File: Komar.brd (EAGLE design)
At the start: 58 x 58 mm, 109 parts, among them CON1 USB-VERTICAL, CON2 PINHEAD_1X01-2, CON3 CON-4P-TABS-STRAIGHT, CON4 CON-4P-TABS-STRAIGHT, CON5 CON-4P-TABS-STRAIGHT, CON6 CON-4P-TABS-STRAIGHT, CON7 CON-4P-TABS-STRAIGHT, CON8 CON-6P-SM06B, CON9 PINHEAD_1X01-2, IC1 TPD3S014DBVR-SOT23-6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

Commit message: CAN transciever replaced due for logistic reasons
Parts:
- IC3, IC4: value TJA1051-HVSON8 -> ATA6561-GBQW-N-HVSON8

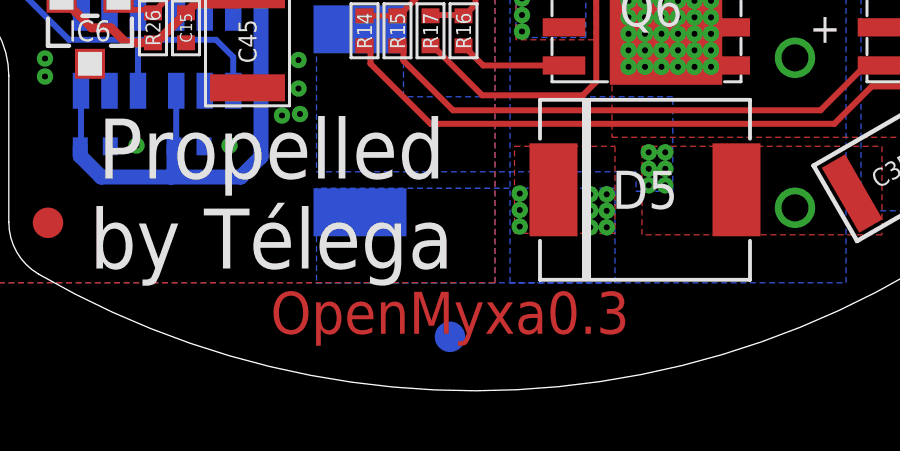
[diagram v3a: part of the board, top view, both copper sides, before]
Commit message: NETs naming updates
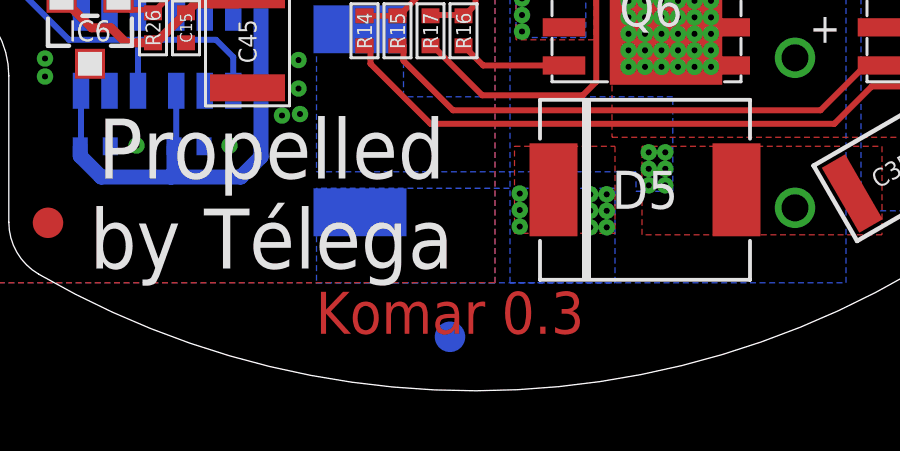
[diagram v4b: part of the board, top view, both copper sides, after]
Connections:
- net N$1 renamed BGH2
- net N$11 renamed AGL1
- net N$12 renamed CGH2
- net N$13 renamed CGL2
- net N$14 renamed CGH1
- net N$15 renamed CGL1
- net N$2 renamed BGL2
- net N$3 renamed BGL1
- net N$4 renamed BGH1
- net N$7 renamed AGH2
- net N$8 renamed AGL2
- net N$9 renamed AGH1
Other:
- board text added: "Komar 0.3"
- board text removed: "OpenMyxa0.3"
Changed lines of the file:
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@@
 <plain>
 <wire x1="29.2" y1="56.85" x2="29.2" y2="1.15" width="0.2" layer="22" style="shortdash"/>
-<text x="28.2" y="2.6" size="1.4" layer="1" font="vector" ratio="15" align="center">OpenMyxa0.3</text>
+<text x="28.2" y="2.6" size="1.4" layer="1" font="vector" ratio="15" align="center">Komar 0.3</text>
 <wire x1="16.5" y1="3.6" x2="40" y2="3.6" width="0.1" layer="49"/>
 <text x="22.25" y="6.575" size="2" layer="21" font="vector" ratio="15" align="center">Propelled
@@
 <wire x1="26.4" y1="45.025" x2="26.475" y2="45.1" width="0.4" layer="1"/>
 </signal>
-<signal name="N$1" class="1">
+<signal name="BGH2" class="1">
 <contactref element="Q1" pad="4"/>
 <contactref element="R2" pad="2"/>
@@
 <wire x1="28" y1="14" x2="28" y2="16" width="0.2" layer="1"/>
 </signal>
-<signal name="N$2">
+<signal name="BGL2">
 <contactref element="Q2" pad="4"/>
 <contactref element="R3" pad="2"/>
@@
 <wire x1="29.05" y1="18.95" x2="28" y2="20" width="0.2" layer="1"/>
 </signal>
-<signal name="N$4" class="1">
+<signal name="BGH1" class="1">
 <contactref element="Q3" pad="4"/>
 <contactref element="R1" pad="2"/>
@@
 <wire x1="26.55" y1="25" x2="27.225" y2="25" width="0.2" layer="16"/>
 </signal>
-<signal name="N$3">
+<signal name="BGL1">
 <contactref element="R4" pad="2"/>
 <contactref element="Q4" pad="4"/>
@@
 <wire x1="24.75" y1="29.8364" x2="24.75" y2="27.1" width="0.2" layer="15"/>
 </signal>
-<signal name="N$7" class="1">
+<signal name="AGH2" class="1">
 <contactref element="Q5" pad="4"/>
 <contactref element="R15" pad="2"/>
@@
 <wire x1="42.045" y1="10.845" x2="40.55" y2="9.35" width="0.2" layer="1"/>
 </signal>
-<signal name="N$8">
+<signal name="AGL2">
 <contactref element="Q6" pad="4"/>
 <contactref element="R16" pad="2"/>
@@
 <wire x1="28.65" y1="11.5" x2="29.305" y2="10.845" width="0.2" layer="1"/>
 </signal>
-<signal name="N$9" class="1">
+<signal name="AGH1" class="1">
 <contactref element="Q7" pad="4"/>
 <contactref element="R14" pad="2"/>
@@
 <wire x1="43.65" y1="16.85" x2="43.3" y2="17.2" width="0.2" layer="1"/>
 </signal>
-<signal name="N$11">
+<signal name="AGL1">
 <contactref element="R17" pad="2"/>
 <contactref element="Q8" pad="4"/>
@@
 <wire x1="23.5" y1="43" x2="23.70606875" y2="43" width="0.15" layer="16"/>
 </signal>
-<signal name="N$12" class="1">
+<signal name="CGH2" class="1">
 <contactref element="Q9" pad="4"/>
 <contactref element="R22" pad="2"/>
@@
 <wire x1="26.375" y1="30.45" x2="26.375" y2="29.8" width="0.15" layer="16"/>
 </signal>
-<signal name="N$13">
+<signal name="CGL2">
 <contactref element="Q10" pad="4"/>
 <contactref element="R23" pad="2"/>
@@
 <wire x1="26.2" y1="26.725425" x2="26.2" y2="28.825" width="0.2" layer="15"/>
 </signal>
-<signal name="N$14" class="1">
+<signal name="CGH1" class="1">
 <contactref element="Q11" pad="4"/>
 <contactref element="R21" pad="2"/>
@@
 <wire x1="42.575" y1="30.525" x2="42.45" y2="30.4" width="0.2" layer="1"/>
 </signal>
-<signal name="N$15">
+<signal name="CGL1">
 <contactref element="R24" pad="2"/>
 <contactref element="Q12" pad="4"/>

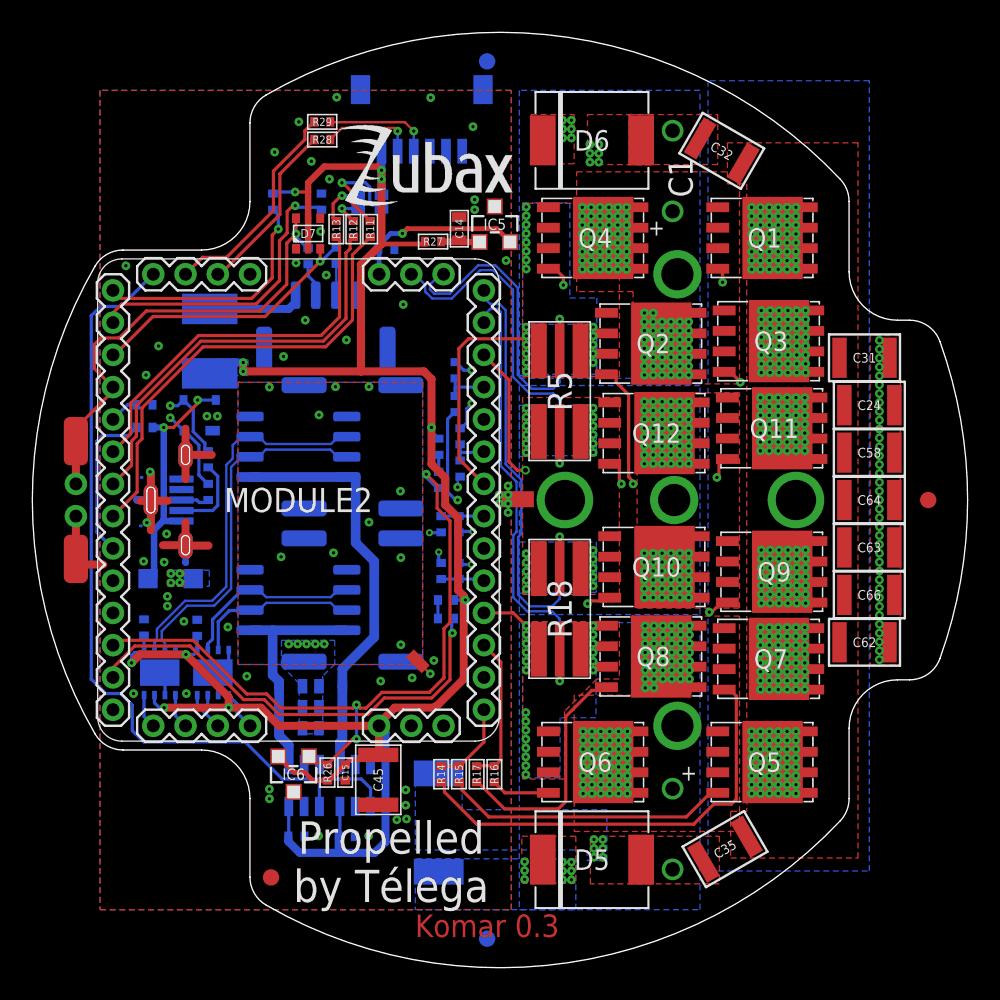
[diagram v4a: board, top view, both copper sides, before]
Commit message: powerstage rerouting partially completed
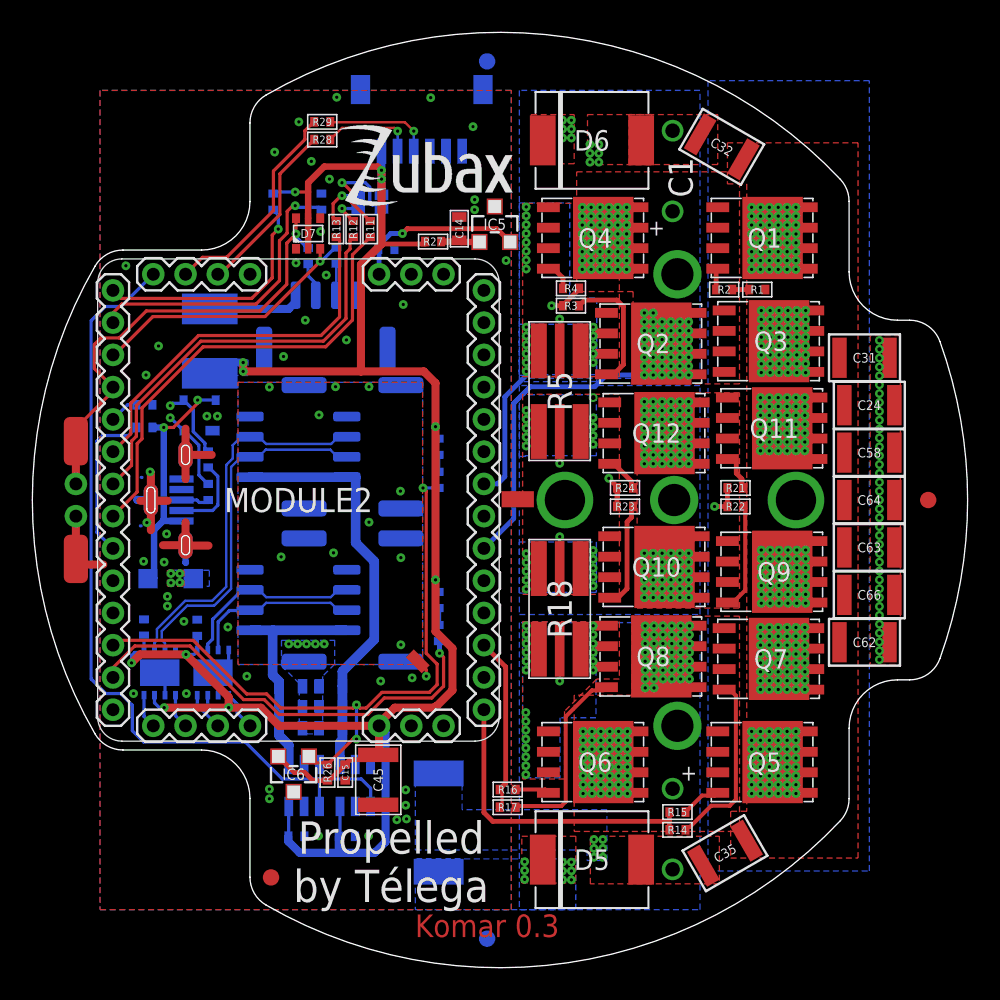
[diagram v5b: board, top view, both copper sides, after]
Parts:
- moved R1 25.4 mm to (45.0, 42.0), flipped to the top, turned to 0 degrees
- moved R2 24.7 mm to (42.9, 42.0), flipped to the top, turned to 180 degrees
- moved R21 17.4 mm to (43.6, 29.8), flipped to the top, turned to 0 degrees
- moved R22 17.2 mm to (43.6, 28.6), flipped to the top, turned to 0 degrees
- moved R4 16.7 mm to (33.4, 42.1), flipped to the top, turned to 180 degrees
- moved R3 15.2 mm to (33.4, 41.0), flipped to the top, turned to 0 degrees
- moved R14 15.1 mm to (40.0, 8.55), turned to 0 degrees
- moved R15 13.8 mm to (40.0, 9.65), turned to 0 degrees
- moved R24 12.8 mm to (36.8, 29.8), flipped to the top, turned to 0 degrees
- moved R23 12.3 mm to (36.8, 28.6), flipped to the top, turned to 0 degrees
- moved S1 6.16 mm to (34.8, 35.4)
- moved R17 2.81 mm to (29.5, 9.95), turned to 0 degrees
- moved R16 1.26 mm to (29.5, 11.1), turned to 0 degrees
- moved R9 1.01 mm to (25.2, 20.8), turned to 90 degrees
- moved LED1 0.45 mm to (25.2, 22.8), turned to 270 degrees
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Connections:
- net BGH2 renamed JHKJ
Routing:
- net JHKJ: track 34.3 -> 1.64 mm, vias 2 -> 0
- net PHASE_B_GATE_HIGH: track 2.69 -> 35.3 mm
- net BGH1: track 28.1 -> 0.00 mm, vias 2 -> 0
- net BGL1: track 25.4 -> 1.79 mm, vias 2 -> 0
- net CGH1: track 23.6 -> 2.39 mm, vias 2 -> 0
- net CGH2: track 26.9 -> 6.65 mm, vias 2 -> 0
- net PHASE_B_GATE_LOW: track 2.65 -> 20.0 mm, vias 0 -> 1
- net CGL1: track 20.0 -> 2.85 mm, vias 2 -> 0
- net PHASE_C_GATE_HIGH: track 2.52 -> 19.0 mm, vias 0 -> 1
- net AGH1: track 27.6 -> 11.2 mm
- net AGH2: track 17.9 -> 2.69 mm
- net CGL2: track 21.3 -> 6.84 mm, vias 2 -> 0
- net PHASE_A_GATE_HIGH: track 5.36 -> 19.2 mm
- net BGL2: track 20.6 -> 7.96 mm, vias 2 -> 0
- net PHASE_C_GATE_LOW: track 3.41 -> 12.0 mm, vias 0 -> 1
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
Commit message: Routing completed
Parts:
- moved R1 0.15 mm to (45.1, 42.0), turned to 180 degrees
- turned R2 to 0 degrees
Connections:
- net JHKJ renamed BGH2
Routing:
- net BGH1: track 0.00 -> 6.24 mm
- net PHASE_B_GATE_HIGH: track 35.3 -> 40.2 mm, vias 0 -> 2
- net CGL1: track 2.85 -> 2.25 mm

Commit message: minor tweaks
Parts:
- moved R3 0.47 mm to (33.8, 40.8)
- moved R4 0.46 mm to (33.8, 41.9)
- moved R21 0.05 mm to (43.6, 29.7)
- moved R24 0.05 mm to (36.8, 29.7)
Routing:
- net LED_RED: track 23.7 -> 23.0 mm
- net LED_GREEN: track 25.9 -> 25.3 mm
- net LED_BLUE: track 28.4 -> 27.8 mm
- net PHASE_B_GATE_LOW: track 20.0 -> 20.6 mm

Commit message: libraries cleanup
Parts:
- S1: device macaroni_masterlib:CURRENT_SHUNT_SENSE -> misc:SENSE-0.6
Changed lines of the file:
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@@
 <setting verticaltext="up"/>
 </settings>
-<grid distance="0.05" unitdist="mm" unit="mm" style="lines" multiple="1" display="yes" altdistance="0.1" altunitdist="mm" altunit="mm"/>
+<grid distance="0.1" unitdist="mm" unit="mm" style="lines" multiple="1" display="yes" altdistance="0.1" altunitdist="mm" altunit="mm"/>
 <layers>
 <layer number="1" name="Top" color="4" fill="1" visible="yes" active="yes"/>
-<layer number="2" name="Route2" color="1" fill="3" visible="yes" active="yes"/>
+<layer number="2" name="Route2" color="1" fill="3" visible="no" active="yes"/>
 <layer number="3" name="Route3" color="4" fill="3" visible="no" active="yes"/>
 <layer number="4" name="Route4" color="1" fill="4" visible="no" active="no"/>
@@
 </layers>
 <board>
-<fusionsync huburn="a.cGVyc29uYWw6dWUyYWE4ZDY4" projecturn="a.cGVyc29uYWw6dWUyYWE4ZDY4IzIwMTgxMDI3MTU2OTA4Mjgx" f3durn="urn:adsk.wipprod:dm.lineage:yua-ROE5Tb29pIDQe9ePEg" pcbguid="" lastpulledtime="" lastsyncedchangeguid="2f929fbb-c978-f929-aad6-dc728fd64175" latestrevisionid="943469be-d66c-497d-be2e-a8540f70ffe4" lastsyncedrevisionid="943469be-d66c-497d-be2e-a8540f70ffe4" lastboardhashguid="89bb0dd0-0cd7-6a5e-7a1a-cabf21d338ab" lastpushedtime="2020-05-12T09:11:51Z" linktopcb3d="%12"/>
 <plain>
 <wire x1="29.2" y1="56.85" x2="29.2" y2="1.15" width="0.2" layer="22" style="shortdash"/>
@@
 <attribute name="TOLERANCE" value="5%" x="-160.25" y="-11.3" size="1.778" layer="27" display="off"/>
 </element>
-<element name="S1" library="macaroni_masterlib" package="CURRENT_SHUNT_SENSE" value="SENSE" x="34.775" y="35.35" smashed="yes">
+<element name="S1" library="misc" library_urn="urn:adsk.eagle:library:5347860" package="SENSE-0.6" package3d_urn="urn:adsk.eagle:package:7365871/1" value="SENSE" x="34.775" y="35.35" smashed="yes">
 <attribute name="BOM" value="EXCLUDE" x="-183.225" y="-31.65" size="1.778" layer="27" display="off"/>
 </element>
@@
 <wire x1="28" y1="26" x2="28.2" y2="26" width="0.3" layer="16"/>
 <wire x1="35.6" y1="36.75" x2="37.95" y2="36.75" width="0.3" layer="16"/>
-<wire x1="29.95" y1="35.1" x2="30.875" y2="36.025" width="0.3" layer="16"/>
-<wire x1="30.875" y1="36.025" x2="34.875" y2="36.025" width="0.3" layer="16"/>
-<wire x1="34.875" y1="36.025" x2="35.6" y2="36.75" width="0.3" layer="16"/>
+<wire x1="29.95" y1="35.1" x2="30.975" y2="36.125" width="0.3" layer="16"/>
+<wire x1="30.975" y1="36.125" x2="34.975" y2="36.125" width="0.3" layer="16"/>
+<wire x1="34.975" y1="36.125" x2="35.6" y2="36.75" width="0.3" layer="16"/>
 <wire x1="28.2" y1="26" x2="29.95" y2="27.75" width="0.3" layer="16"/>
 <wire x1="29.95" y1="27.75" x2="29.95" y2="35.1" width="0.3" layer="16"/>
@@
 </note>
 <note version="8.3" severity="warning">
-Since Version 8.3, EAGLE supports Fusion synchronisation.
-This feature will not be available in this version and saving
-the document will break the link to the Fusion PCB feature.
-</note>
-<note version="8.3" severity="warning">
